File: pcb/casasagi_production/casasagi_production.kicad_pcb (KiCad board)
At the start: 2 copper layers, 268.4 x 96.7 mm, 238 parts, among them J101 USB_C_Receptacle_USB2.0, J102 AudioJack4, J103 Conn_01x05, J201 USB_C_Receptacle_USB2.0, J202 AudioJack4, J203 Conn_01x05, SW101 RESET, SW102 BOOT, SW201 RESET, SW202 BOOT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

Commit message: add fiducial mark
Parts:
- added REF**: Fiducial_1.5mm_Mask4.5mm, Fiducial:Fiducial_1.5mm_Mask4.5mm, B.Cu at (293.8, 121.2)
- added REF**: Fiducial_1.5mm_Mask4.5mm, Fiducial:Fiducial_1.5mm_Mask4.5mm, B.Cu at (50.8, 30.0)
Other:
- board text added: "Casasagi pcb / Rev. Alpha"

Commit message: prepare pcb for BOM and add BOM left
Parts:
- removed the REF** at (293.8, 121.2)
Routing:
- net GND: vias 295 -> 297
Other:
- outline, holes or cut-outs redrawn

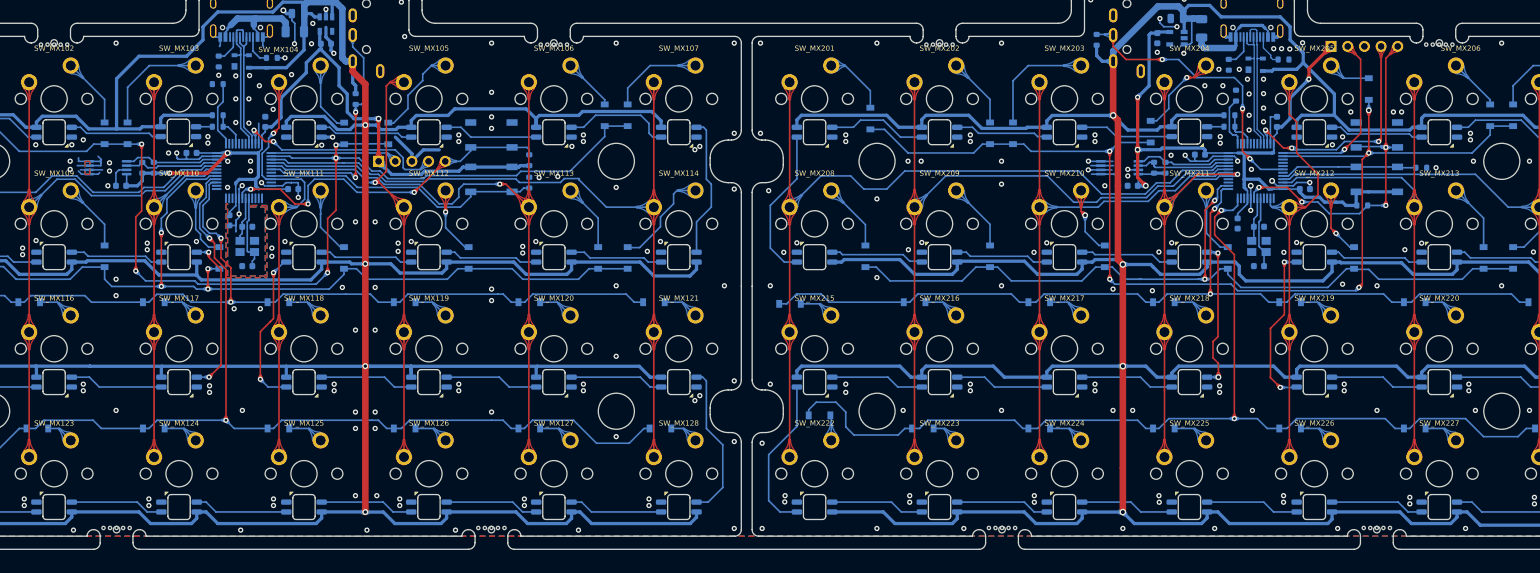
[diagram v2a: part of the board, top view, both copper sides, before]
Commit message: update mousebite
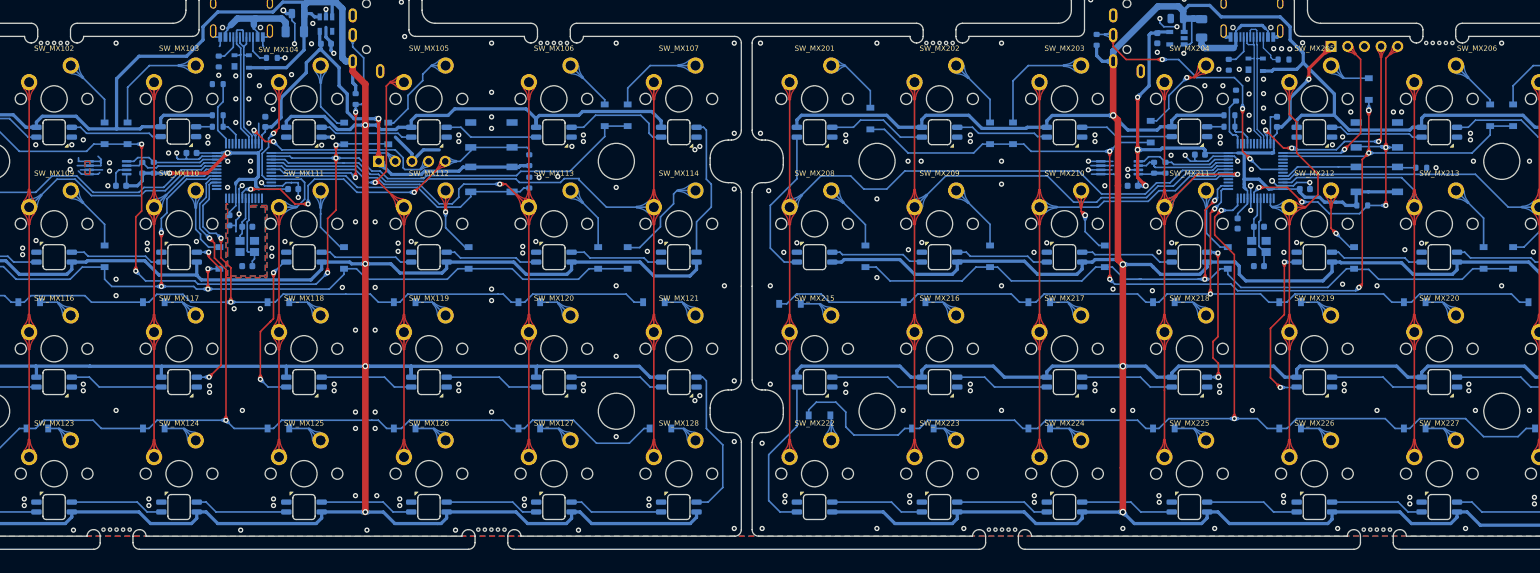
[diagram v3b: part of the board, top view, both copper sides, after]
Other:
- outline, holes or cut-outs redrawn

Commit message: add rev.alpha production pcb
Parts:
- removed the REF** at (270.7, 115.7)
- removed the REF** at (213.6, 115.7)
- removed the REF** at (135.7, 115.7)
- removed the REF** at (78.6, 115.7)
- removed the REF** at (280.2, 41.5)
- removed the REF** at (204.1, 41.5)
- removed the REF** at (145.2, 41.5)
- removed the REF** at (69.0, 41.5)
- removed the REF** at (50.8, 30.0)
- added REF**: Fiducial_1mm_Mask2mm, Fiducial:Fiducial_1mm_Mask2mm, B.Cu at (158.8, 206.2)
- added REF**: MOUSEBITE_5mm, dm9_drill_hole:MOUSEBITE_5mm, F.Cu at (55.5, 41.5)
- added REF**: Fiducial_1mm_Mask2mm, Fiducial:Fiducial_1mm_Mask2mm, B.Cu at (50.5, 28.5)
- added REF**: MOUSEBITE_5mm, dm9_drill_hole:MOUSEBITE_5mm, F.Cu at (158.8, 200.7)
- added REF**: MOUSEBITE_5mm, dm9_drill_hole:MOUSEBITE_5mm, F.Cu at (55.5, 200.7)
- added REF**: MOUSEBITE_5mm, dm9_drill_hole:MOUSEBITE_5mm, F.Cu at (55.5, 126.5)
- added REF**: MOUSEBITE_5mm, dm9_drill_hole:MOUSEBITE_5mm, F.Cu at (55.5, 115.7)
- added REF**: MOUSEBITE_5mm, dm9_drill_hole:MOUSEBITE_5mm, F.Cu at (158.8, 126.5)
- added REF**: MOUSEBITE_5mm, dm9_drill_hole:MOUSEBITE_5mm, F.Cu at (158.8, 115.7)
- added REF**: MOUSEBITE_5mm, dm9_drill_hole:MOUSEBITE_5mm, F.Cu at (158.8, 41.5)
- moved SW201 159.5 mm to (135.7, 140.5)
- moved SW202 159.5 mm to (135.7, 147.3)
- moved C201 159.5 mm to (105.2, 122.8)
- moved C202 159.5 mm to (102.2, 125.8)
- moved C203 159.5 mm to (98.5, 148.2)
- moved C204 159.5 mm to (117.8, 160.5)
- moved C205 159.5 mm to (114.5, 154.0)
- moved C206 159.5 mm to (108.8, 143.5)
- moved C207 159.5 mm to (120.5, 138.5)
- moved C208 159.5 mm to (124.8, 148.8)
- moved C209 159.5 mm to (117.8, 154.5)
- moved D201 159.5 mm to (117.2, 129.8)
- moved D202 159.5 mm to (58.5, 138.0)
- moved D203 159.5 mm to (76.8, 140.2)
- moved D204 159.5 mm to (80.2, 140.2)
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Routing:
- net GND: track 131.2 -> 138.8 mm
- net +5V: track 1303.9 -> 1305.2 mm
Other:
- board size 268.4 x 96.7 mm -> 133.3 x 182.7 mm
- rule pad_to_mask_clearance: 0.1 -> 0
- board text removed: "Casasagi pcb / Rev. Alpha"
